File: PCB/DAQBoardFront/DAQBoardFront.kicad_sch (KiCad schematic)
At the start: 25 parts, among them J2 53375-0410, U5 TCAN1051VDRQ1

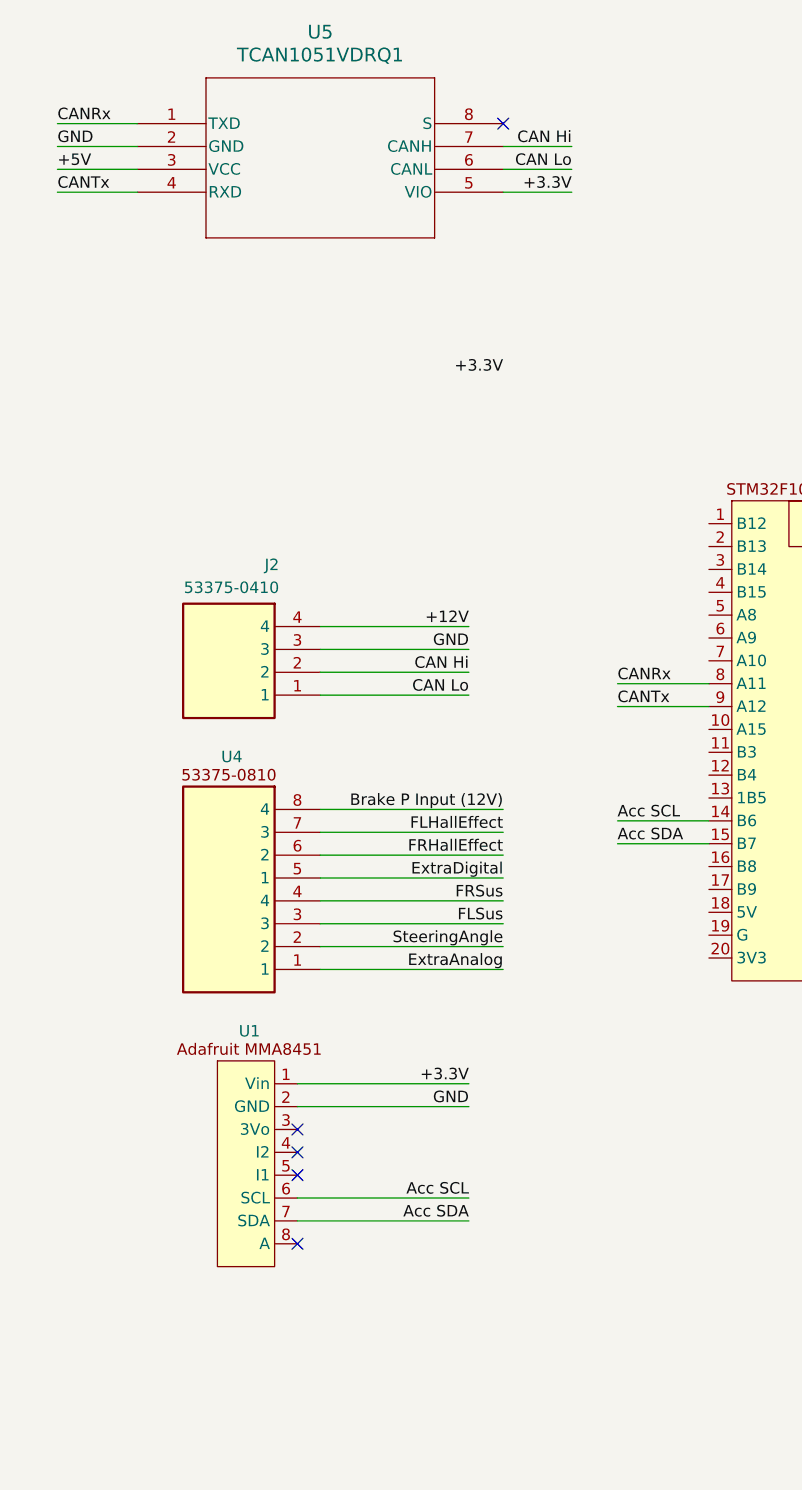
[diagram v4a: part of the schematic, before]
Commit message: Began restructuring dash PCB, migrated footprints & symbols to the central library
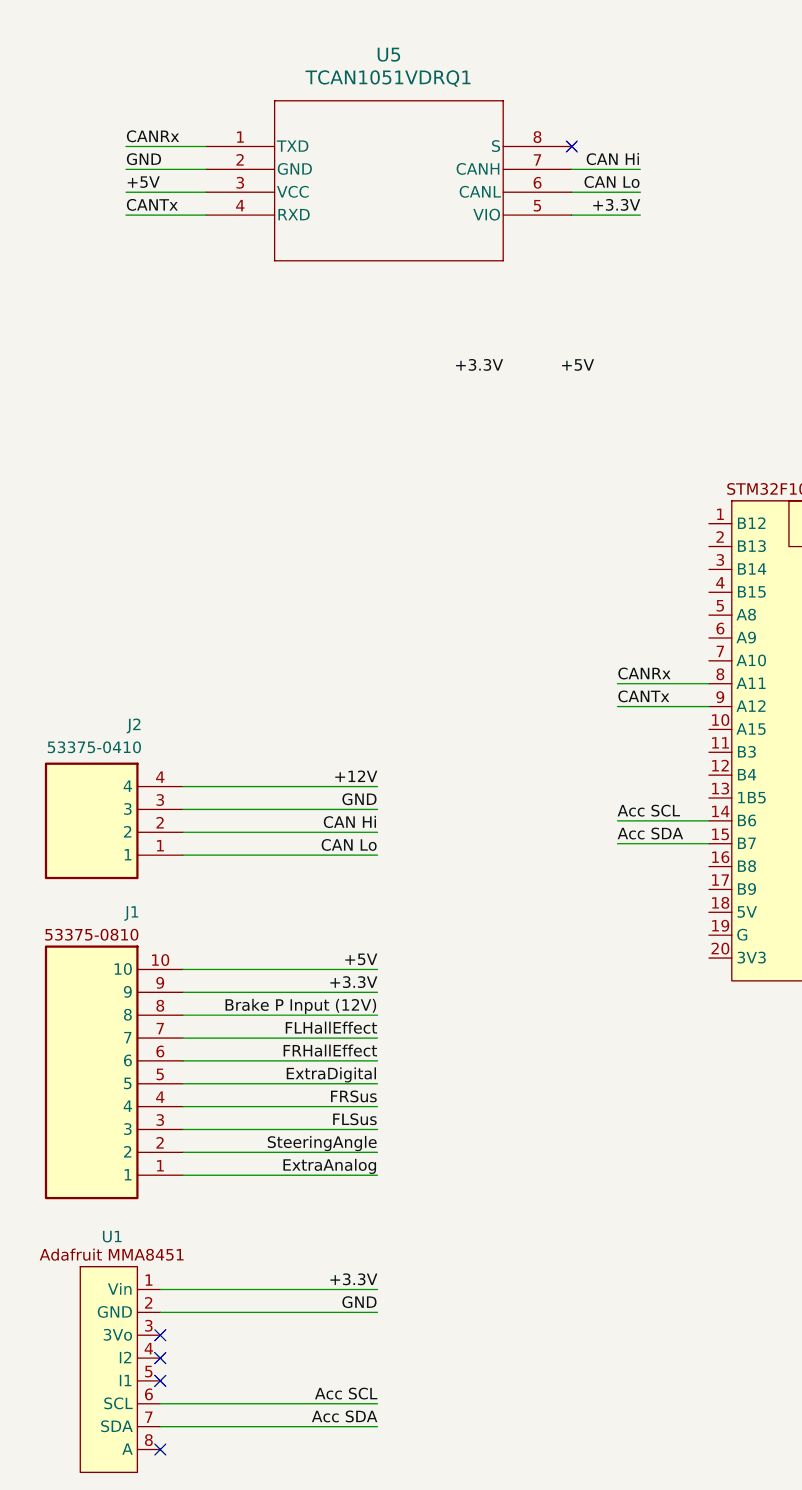
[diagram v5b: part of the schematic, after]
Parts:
- removed U4: (no value), CFR-Footprint-Library:CONN08_533750810_MOL, symbol CFR-Symbol-Library:53375-0810
- added J1: (no value), CONN10_533751010_MOL, symbol CFR Library:53375-1010
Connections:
- net +3.3V: now also J1.9
- net +5V: now also J1.10
- net Brake P Input (12V): now also J1.8
- net ExtraAnalog: now also J1.1
- net ExtraDigital: now also J1.5
- net FLHallEffect: now also J1.7
- net FLSus: now also J1.3
- net FRHallEffect: now also J1.6
- net FRSus: now also J1.4
- net SteeringAngle: now also J1.2
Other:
- moved on the sheet: J2, U1, U5

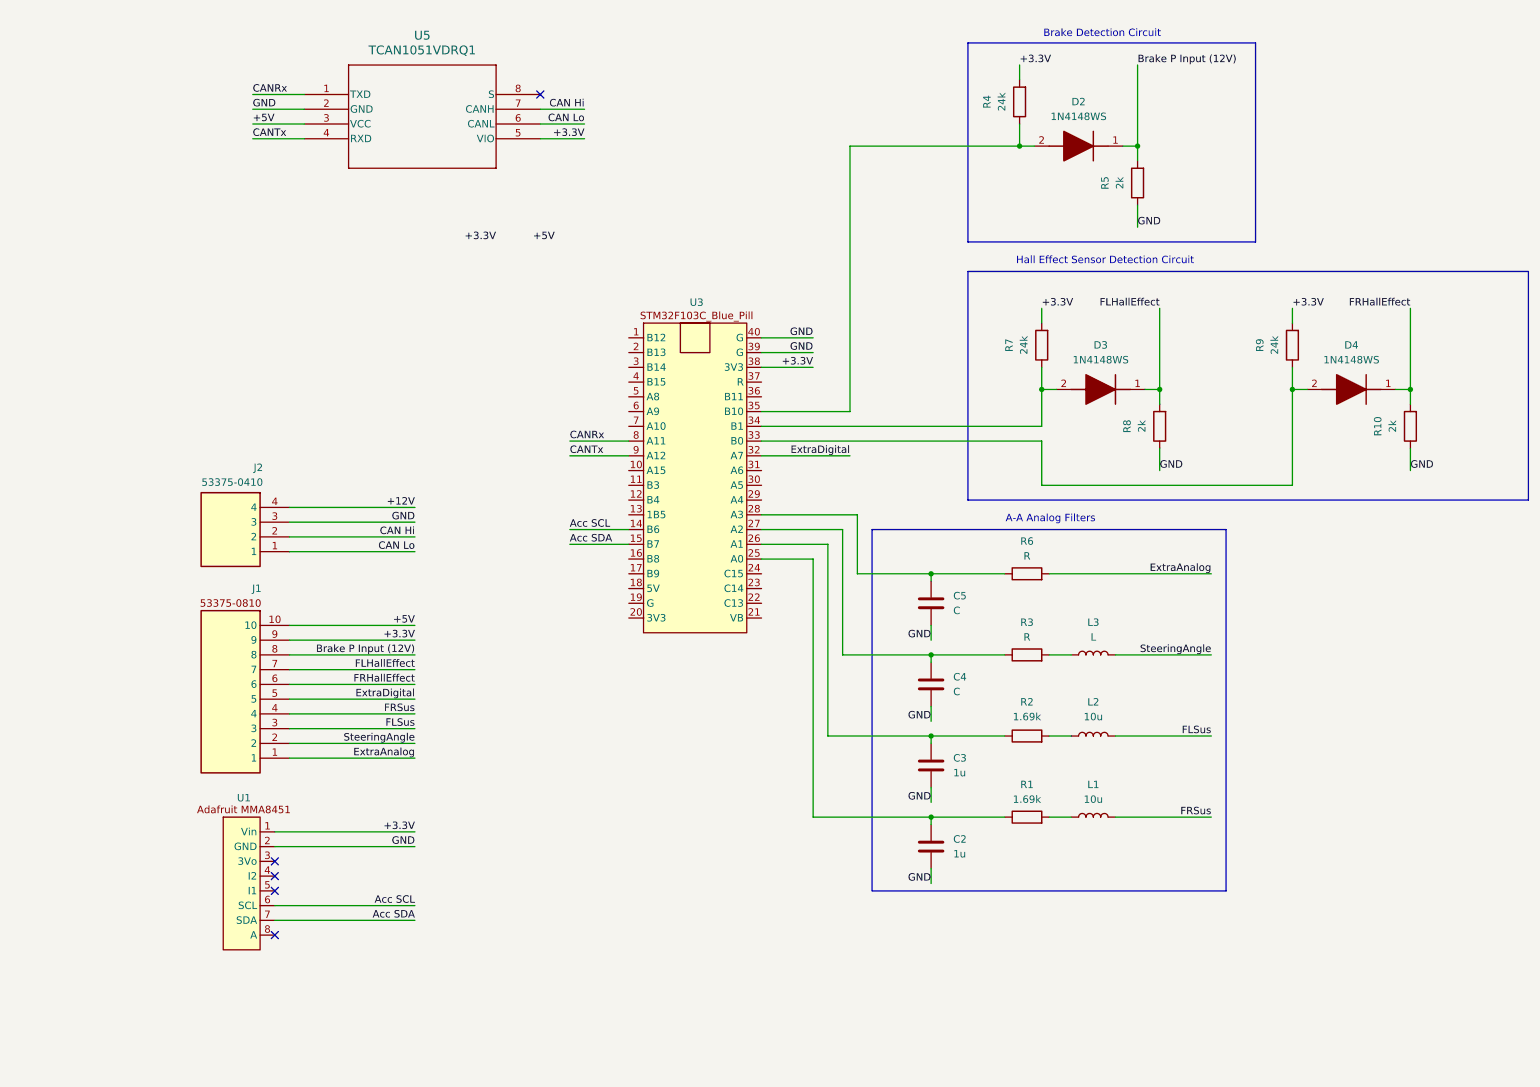
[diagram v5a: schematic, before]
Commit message: Slightly restructured dashboard, updated daq board schematic with buck converter and can module
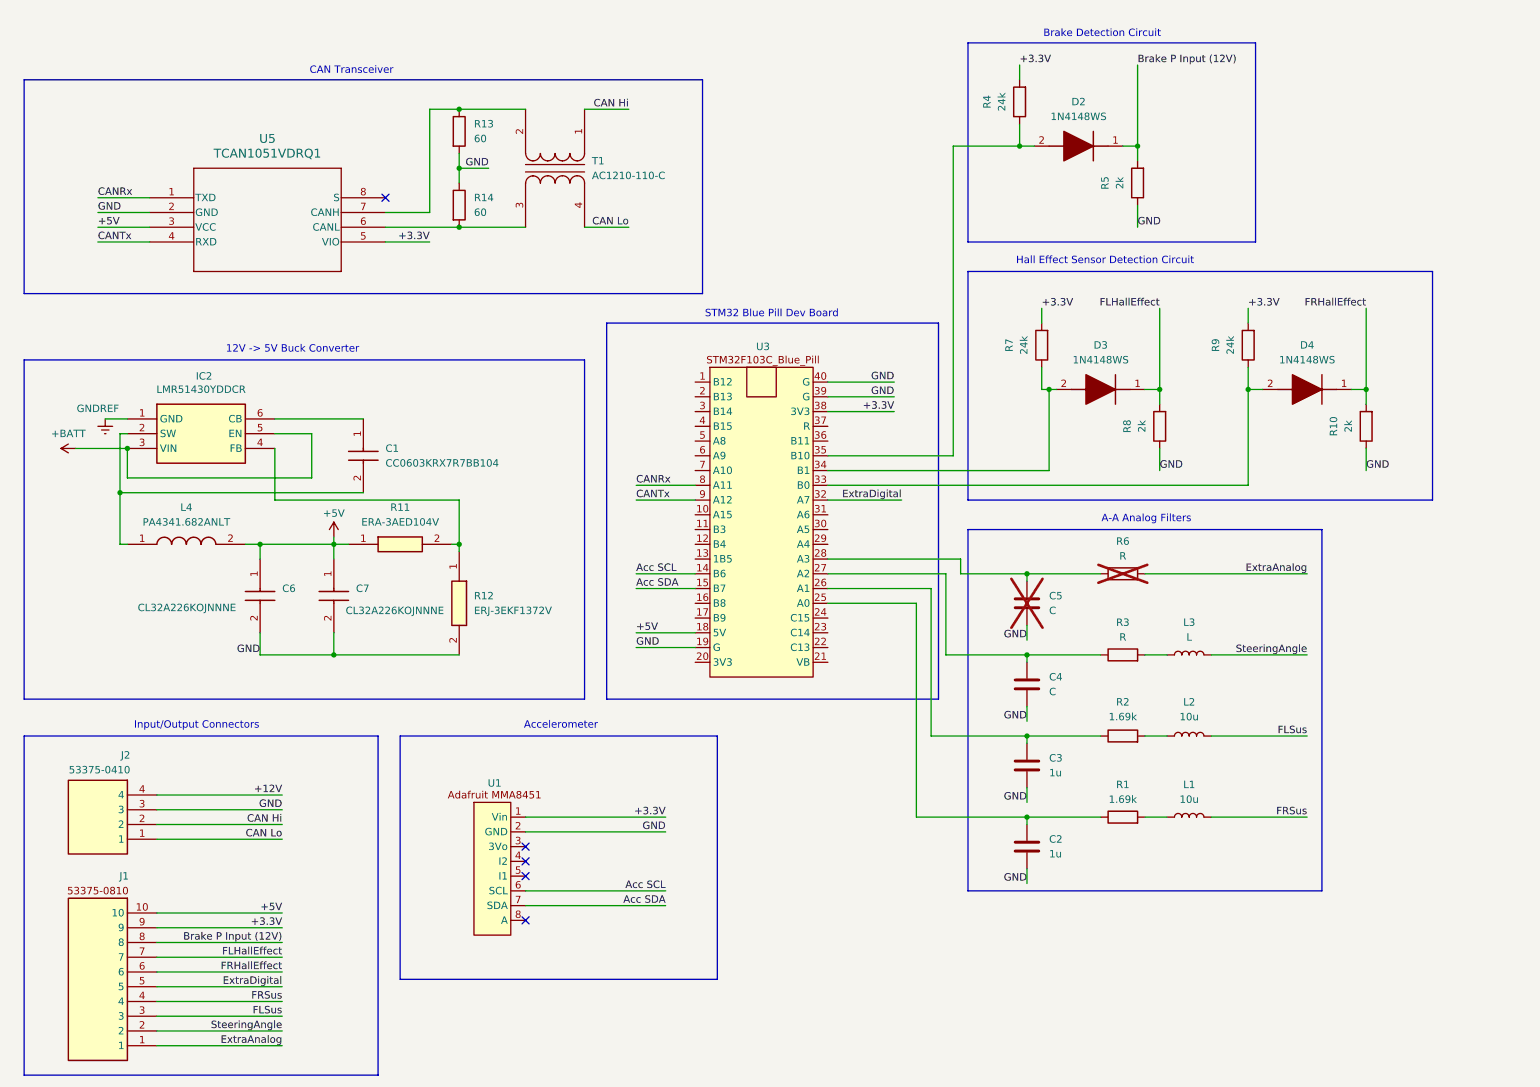
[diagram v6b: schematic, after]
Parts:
- added C1: CC0603KRX7R7BB104, Capacitor_SMD:C_0603_1608Metric, symbol CFR Library:CL05B104KO5NNNC
- added C6, C7: CL32A226KOJNNNE, Capacitor_SMD:C_1210_3225Metric, symbol CFR Library:CL32A226KOJNNNE
- added IC2: LMR51430YDDCR, CFR Library:SOT95P280X110-6N, symbol CFR Library:LMR51430YDDCR
- added L4: PA4341.682ANLT, CFR Library:INDPM7166X300N, symbol CFR Library:PA4341.682ANLT
- added R11: ERA-3AED104V, Resistor_SMD:R_0603_1608Metric, symbol CFR Library:ERA-3AED104V
- added R12: ERJ-3EKF1372V, Resistor_SMD:R_0603_1608Metric, symbol CFR Library:ERJ-3EKF1372V
- added R13, R14: 60, Resistor_SMD:R_0603_1608Metric, symbol Device:R
- added T1: AC1210-110-C, CFR Library:AC1210-110-C, symbol Device:Transformer_1P_1S
- C5, R6: now not fitted
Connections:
- net +5V: now also U3.18 (5V), C6.1, C7.1, L4.2, R11.1
- net CAN Hi: now also T1.1 (AA); no longer U5.7 (CANH)
- net CAN Lo: now also T1.4 (SB); no longer U5.6 (CANL)
- net GND: now also U3.19 (G), C6.2, C7.2, R12.2, R13.2, R14.1
- new net: R13.1, T1.2 (AB), U5.7 (CANH)
- new net: R14.2, T1.3 (SA), U5.6 (CANL)
- new net: C1.2, IC2.2 (SW), L4.1
- new net: IC2.4 (FB), R11.2, R12.1
- new net: C1.1, IC2.6 (CB)
- new net +BATT: IC2.3 (VIN), IC2.5 (EN)
- new net GNDREF: IC2.1 (GND)
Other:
- note added: "12V -> 5V Buck Converter"
- note added: "Accelerometer"
- note added: "CAN Transceiver"
- note added: "Input/Output Connectors"
- note added: "STM32 Blue Pill Dev Board"
- title: (none) -> Data Acquisition Module
- moved on the sheet: C2, C3, C4, D4, J1, J2, L1, L2, L3, R1, R10, R2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

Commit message: Sized buck converter traces, began re-routing DAQ board
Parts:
- IC2: footprint CFR Library:SOT95P280X110-6N -> CFR-Footprint-Library:SOT95P280X110-6N
- L4: footprint CFR Library:INDPM7166X300N -> CFR-Footprint-Library:INDPM7166X300N
- T1: footprint CFR Library:AC1210-110-C -> CFR-Footprint-Library:AC1210-110-C
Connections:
- net +BATT is gone; now on net +12V: IC2.3 (VIN), IC2.5 (EN)
- net GNDREF is gone; now on net GND: IC2.1 (GND)
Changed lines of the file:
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@@
 		)
 	)
+	(label "GND"
+		(at 29.21 81.28 180)
+		(effects
+			(font
+				(size 1.27 1.27)
+			)
+			(justify right bottom)
+		)
+	)
 	(label "+3.3V"
 		(at 165.1 80.01 180)
@@
 		)
 	)
+	(label "+12V"
+		(at 24.13 86.36 0)
+		(effects
+			(font
+				(size 1.27 1.27)
+			)
+			(justify left bottom)
+		)
+	)
 	(label "GND"
 		(at 187.96 147.32 180)
@@
 			)
 		)
-		(property "Footprint" "CFR Library:AC1210-110-C"
+		(property "Footprint" "CFR-Footprint-Library:AC1210-110-C"
 			(at 106.68 38.1 0)
 			(hide yes)
@@
 			)
 		)
-		(property "Footprint" "CFR Library:SOT95P280X110-6N"
+		(property "Footprint" "CFR-Footprint-Library:SOT95P280X110-6N"
 			(at 54.61 176.2 0)
 			(hide yes)
@@
 			)
 		)
-		(property "Footprint" "CFR Library:INDPM7166X300N"
+		(property "Footprint" "CFR-Footprint-Library:INDPM7166X300N"
 			(at 49.53 199.06 0)
 			(hide yes)
@@
 	)
 	(symbol
-		(lib_id "power:GNDREF")
-		(at 29.21 81.28 0)
-		(unit 1)
-		(body_style 1)
-		(exclude_from_sim no)
-		(in_bom yes)
-		(on_board yes)
-		(in_pos_files yes)
-		(dnp no)
-		(property "Reference" "#PWR04"
-			(at 29.21 87.63 0)
-			(hide yes)
-			(show_name no)
-			(do_not_autoplace no)
-			(effects
-				(font
-					(size 1.27 1.27)
-				)
-			)
-		)
-		(property "Value" "GNDREF"
-			(at 27.94 79.502 0)
-			(show_name no)
-			(do_not_autoplace no)
-			(effects
-				(font
-					(size 1.27 1.27)
-				)
-			)
-		)
-		(property "Footprint" ""
-			(at 29.21 81.28 0)
-			(hide yes)
-			(show_name no)
-			(do_not_autoplace no)
-			(effects
-				(font
-					(size 1.27 1.27)
-				)
-			)
-		)
-		(property "Datasheet" ""
-			(at 29.21 81.28 0)
-			(hide yes)
-			(show_name no)
-			(do_not_autoplace no)
-			(effects
-				(font
-					(size 1.27 1.27)
-				)
-			)
-		)
-		(property "Description" "Power symbol creates a global label with name \"GNDREF\" , reference supply ground"
-			(at 29.21 81.28 0)
-			(hide yes)
-			(show_name no)
-			(do_not_autoplace no)
-			(effects
-				(font
-					(size 1.27 1.27)
-				)
-			)
-		)
-		(pin "1"
-		)
-		(instances
-			(project "DAQBoardFront"
-				(path "/b8c14199-b7a8-42b0-9649-393d2e0c6b59"
-					(reference "#PWR04")
-					(unit 1)
-				)
-			)
-		)
-	)
-	(symbol
 		(lib_id "Device:C")
 		(at 187.96 113.03 0)
@@
 					(unit 1)
 				)
-			)
-		)
-	)
-	(symbol
-		(lib_id "power:+BATT")
-		(at 24.13 86.36 90)
-		(unit 1)
-		(body_style 1)
-		(exclude_from_sim no)
-		(in_bom yes)
-		(on_board yes)
-		(in_pos_files yes)
-		(dnp no)
-		(fields_autoplaced yes)
-		(property "Reference" "#PWR014"
-			(at 27.94 86.36 0)
-			(hide yes)
-			(show_name no)
-			(do_not_autoplace no)
-			(effects
-				(font
-					(size 1.27 1.27)
-				)
-			)
-		)
-		(property "Value" "+BATT"
-			(at 22.86 83.82 90)
-			(show_name no)
-			(do_not_autoplace no)
-			(effects
-				(font
-					(size 1.27 1.27)
-				)
-			)
-		)
-		(property "Footprint" ""
-			(at 24.13 86.36 0)
-			(hide yes)
-			(show_name no)
-			(do_not_autoplace no)
-			(effects
-				(font
-					(size 1.27 1.27)
-				)
-			)
-		)
-		(property "Datasheet" ""
-			(at 24.13 86.36 0)
-			(hide yes)
-			(show_name no)
-			(do_not_autoplace no)
-			(effects
-				(font
-					(size 1.27 1.27)
-				)
-			)
-		)
-		(property "Description" "Power symbol creates a global label with name \"+BATT\""
-			(at 24.13 86.36 0)
-			(hide yes)
-			(show_name no)
-			(do_not_autoplace no)
-			(effects
-				(font
-					(size 1.27 1.27)
-				)
-			)
-		)
-		(pin "1"
-		)
-		(instances
-			(project "DAQBoardFront"
-				(path "/b8c14199-b7a8-42b0-9649-393d2e0c6b59"
-					(reference "#PWR014")
-					(unit 1)
-				)
